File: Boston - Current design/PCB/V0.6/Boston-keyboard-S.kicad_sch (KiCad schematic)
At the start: 599 parts, among them J701 Conn_01x02_Female, J702 Conn_01x03_Female, J705 TYPE-C-31-M12_13, J706 Conn_ARM_JTAG_SWD_10, Q701 DTC123J, Q702 AO4406AL, SW1 MXSwitch, SW10 MXSwitch, SW100 MXSwitch, SW101 MXSwitch, SW102 MXSwitch, SW103 MXSwitch, SW104 MXSwitch, SW105-1 MXSwitch, SW105-2 MXSwitch, SW106 MXSwitch, SW107 MXSwitch, SW108 MXSwitch, SW109 MXSwitch, SW11 MXSwitch, SW110 MXSwitch, SW111 MXSwitch, SW112 MXSwitch, SW113 MXSwitch, SW114 MXSwitch, SW115 MXSwitch, SW116 MXSwitch, SW117 MXSwitch, SW118 MXSwitch, SW119 MXSwitch, SW12 MXSwitch, SW120 MXSwitch, SW121 MXSwitch, SW122 MXSwitch, SW123 MXSwitch, SW124-1 MXSwitch, SW124-2 MXSwitch, SW125 MXSwitch, SW126 Rotary_Encoder_Switch_Chassis, SW127 MXSwitch, SW128 MXSwitch, SW129 MXSwitch, SW13 MXSwitch, SW14 MXSwitch, SW15 MXSwitch, SW16 MXSwitch, SW17 MXSwitch, SW18 MXSwitch, SW19 MXSwitch, SW2 MXSwitch, SW20-1 MXSwitch, SW20-2 MXSwitch, SW200 SW_Push, SW21 MXSwitch, SW22 MXSwitch, SW23 MXSwitch, SW24 MXSwitch, SW25 MXSwitch, SW26 MXSwitch, SW27 MXSwitch, SW28 MXSwitch, SW29 MXSwitch, SW3 MXSwitch, SW30 MXSwitch, SW31 MXSwitch, SW32 MXSwitch, SW33 MXSwitch, SW34 MXSwitch, SW35 MXSwitch, SW36 MXSwitch, SW37 MXSwitch, SW38 MXSwitch, SW39-1 MXSwitch, SW39-2 MXSwitch, SW39-3 MXSwitch, SW4-1 MXSwitch, SW4-2 MXSwitch, SW40 MXSwitch, SW41 MXSwitch, SW42 MXSwitch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

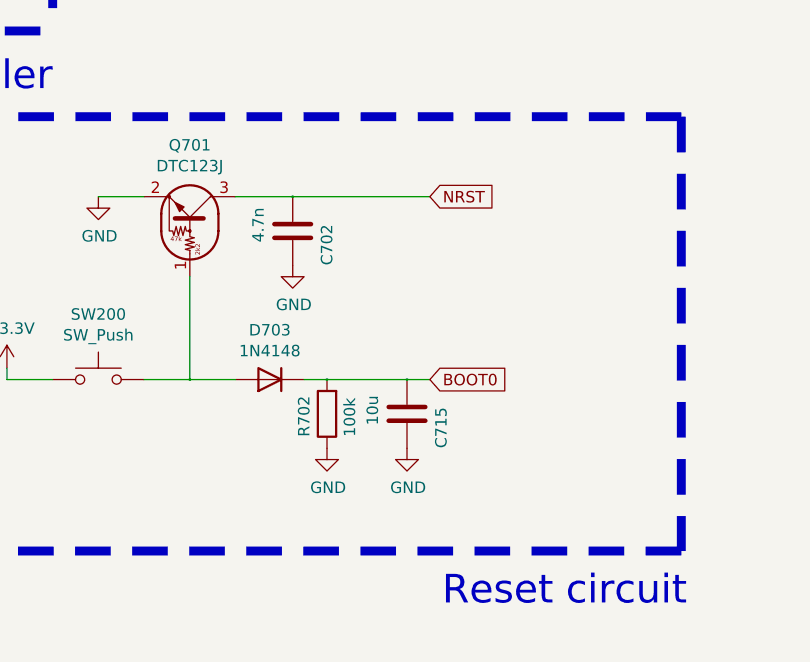
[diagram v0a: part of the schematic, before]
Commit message: More EMI-related layout work
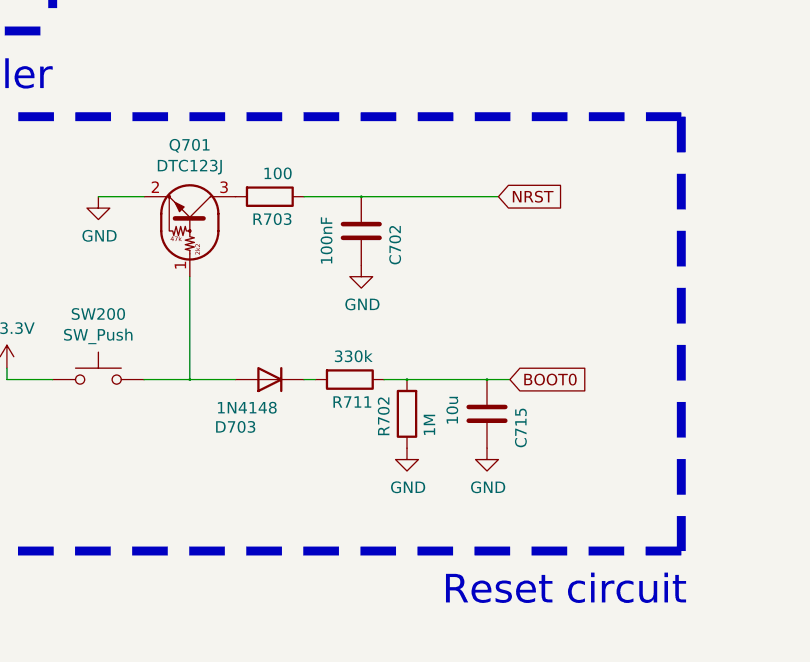
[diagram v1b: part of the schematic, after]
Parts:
- added R703: 100, Resistor_SMD:R_0805_2012Metric_Pad1.15x1.40mm_HandSolder, symbol Device:R
- added R711: 330k, Resistor_SMD:R_0805_2012Metric_Pad1.15x1.40mm_HandSolder, symbol Device:R
- C702: value 4.7n -> 100nF
- R702: value 100k -> 1M
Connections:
- net BOOT0: now also R711.1; no longer D703.1 (K)
- net NRST: now also R703.1; no longer Q701.3 (C)
- new net: Q701.3 (C), R703.2
- new net: D703.1 (K), R711.2
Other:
- moved on the sheet: C702, C715, R702

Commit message: Ran DRC, checked everything over
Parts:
- R1, R10, R100, R101, R102, R103, R104, R1051, R1052, R106, R107, R108, R109, R11, R110, R111, R112, R113, R114, R115, R116, R117, R118, R119, R12, R120, R121, R122, R123, R1241, R1242, R125, R127, R128, R129, R13, R14, R15, R16, R17, R18, R19, R2, R20, R21, R22, R23, R24, R25, R26, R27, R28, R29, R3, R30, R31, R32, R33, R34, R35, R36, R37, R38, R39, R4, R40, R41, R42, R43, R44, R45, R46, R47, R48, R49, R50, R501, R502, R51, R52, R53, R54, R55, R56, R57, R58, R59, R6, R60, R61, R62, R63, R64, R65, R66, R67, R68, R69, R7, R70, R703, R706, R71, R710, R72, R73, R74, R75, R76, R77, R78, R79, R8, R80, R81, R82, R83, R84, R85, R86, R87, R881, R882, R89, R9, R901, R902, R91, R92, R93, R94, R95, R96, R97, R98, R99: value 100 -> 100 1%
- R702: value 1M -> 1M 1%
- R711: value 330k -> 330k 1%
